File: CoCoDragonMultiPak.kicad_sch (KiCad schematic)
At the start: 51 parts, among them CN5 ATX-24, IC1 74LS245, IC10 74LS74, IC11 74LS153, IC12 74ALS30, IC13 GAL16V8, IC2 74LS367, IC3 74LS367, IC4 74LS367, IC5 74LS367, IC6 74LS367, IC7 74LS374, IC8 74LS368, IC9 74LS139, J1 CARTRIDGE EDGE, J2 CARTRIDGE EDGE, J3 CARTRIDGE EDGE, J4 CARTRIDGE EDGE, J5 CARTRIDGE EDGE, SW1 DEFAULT SLOT

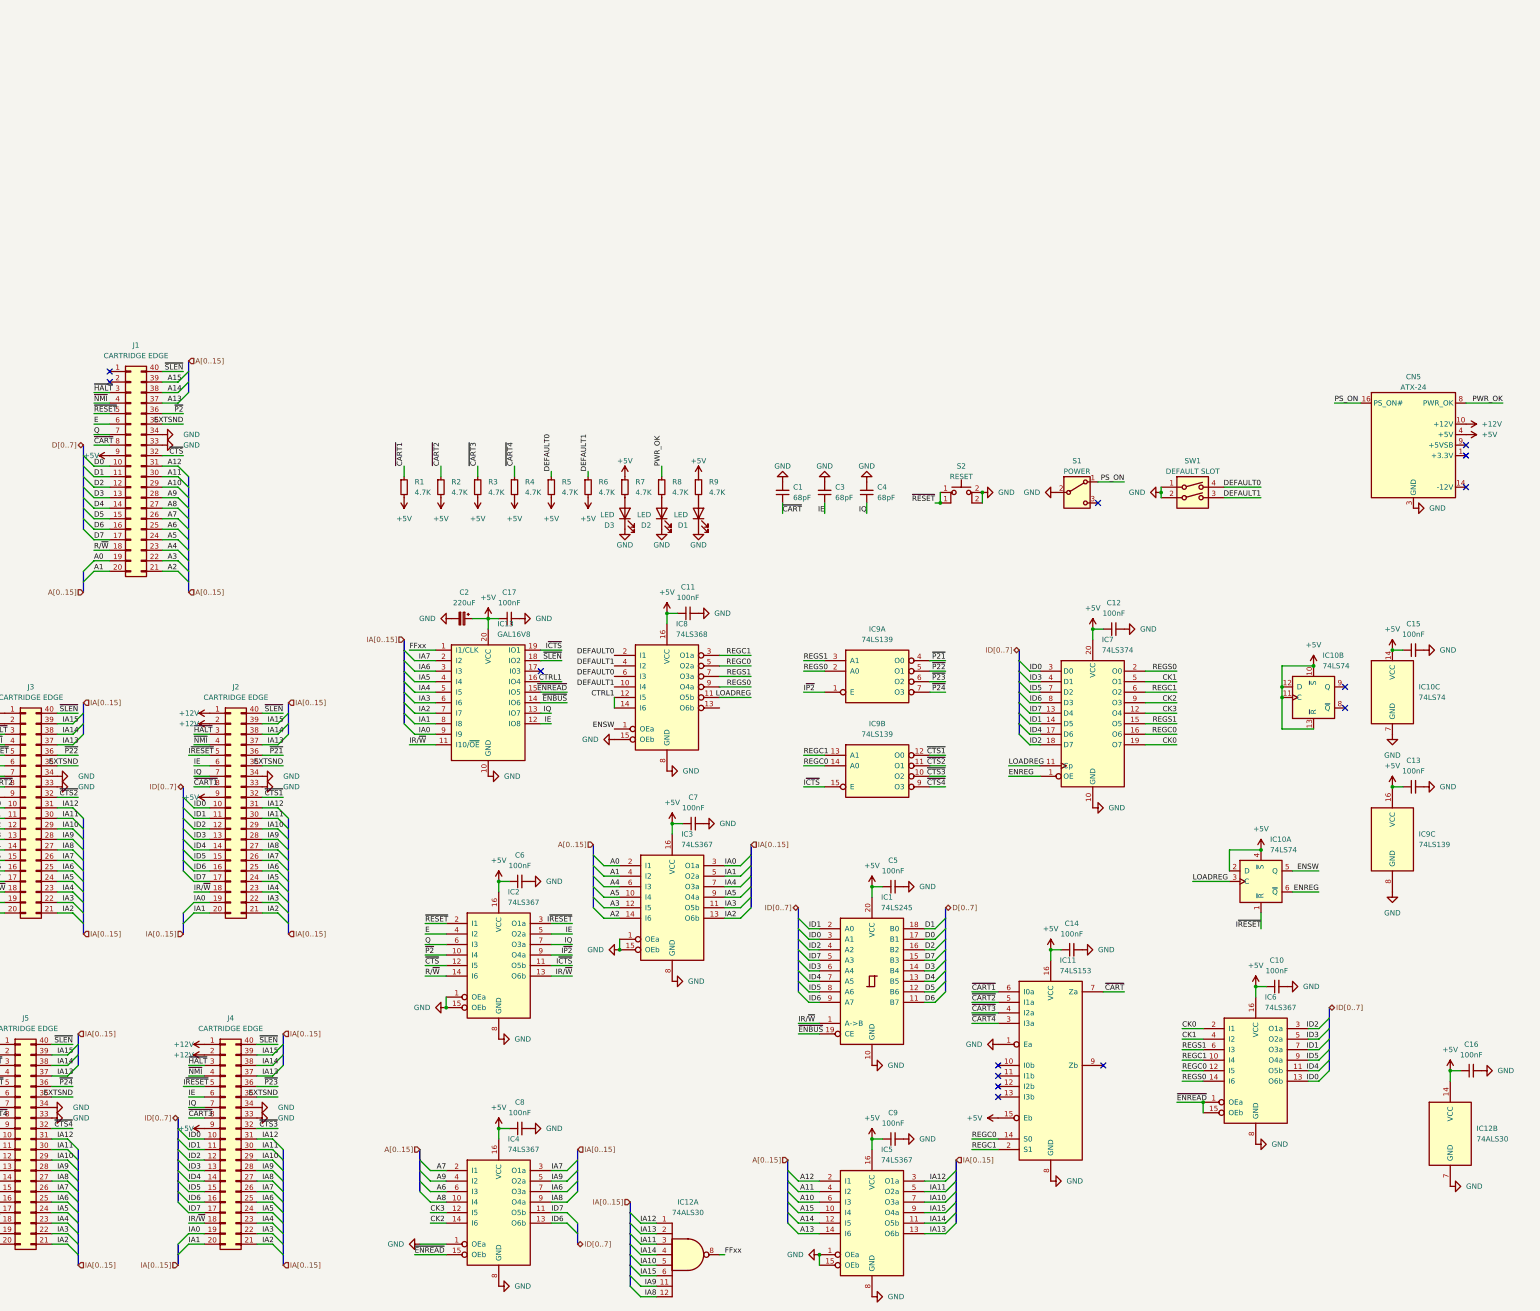
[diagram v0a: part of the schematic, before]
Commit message: convert to smd
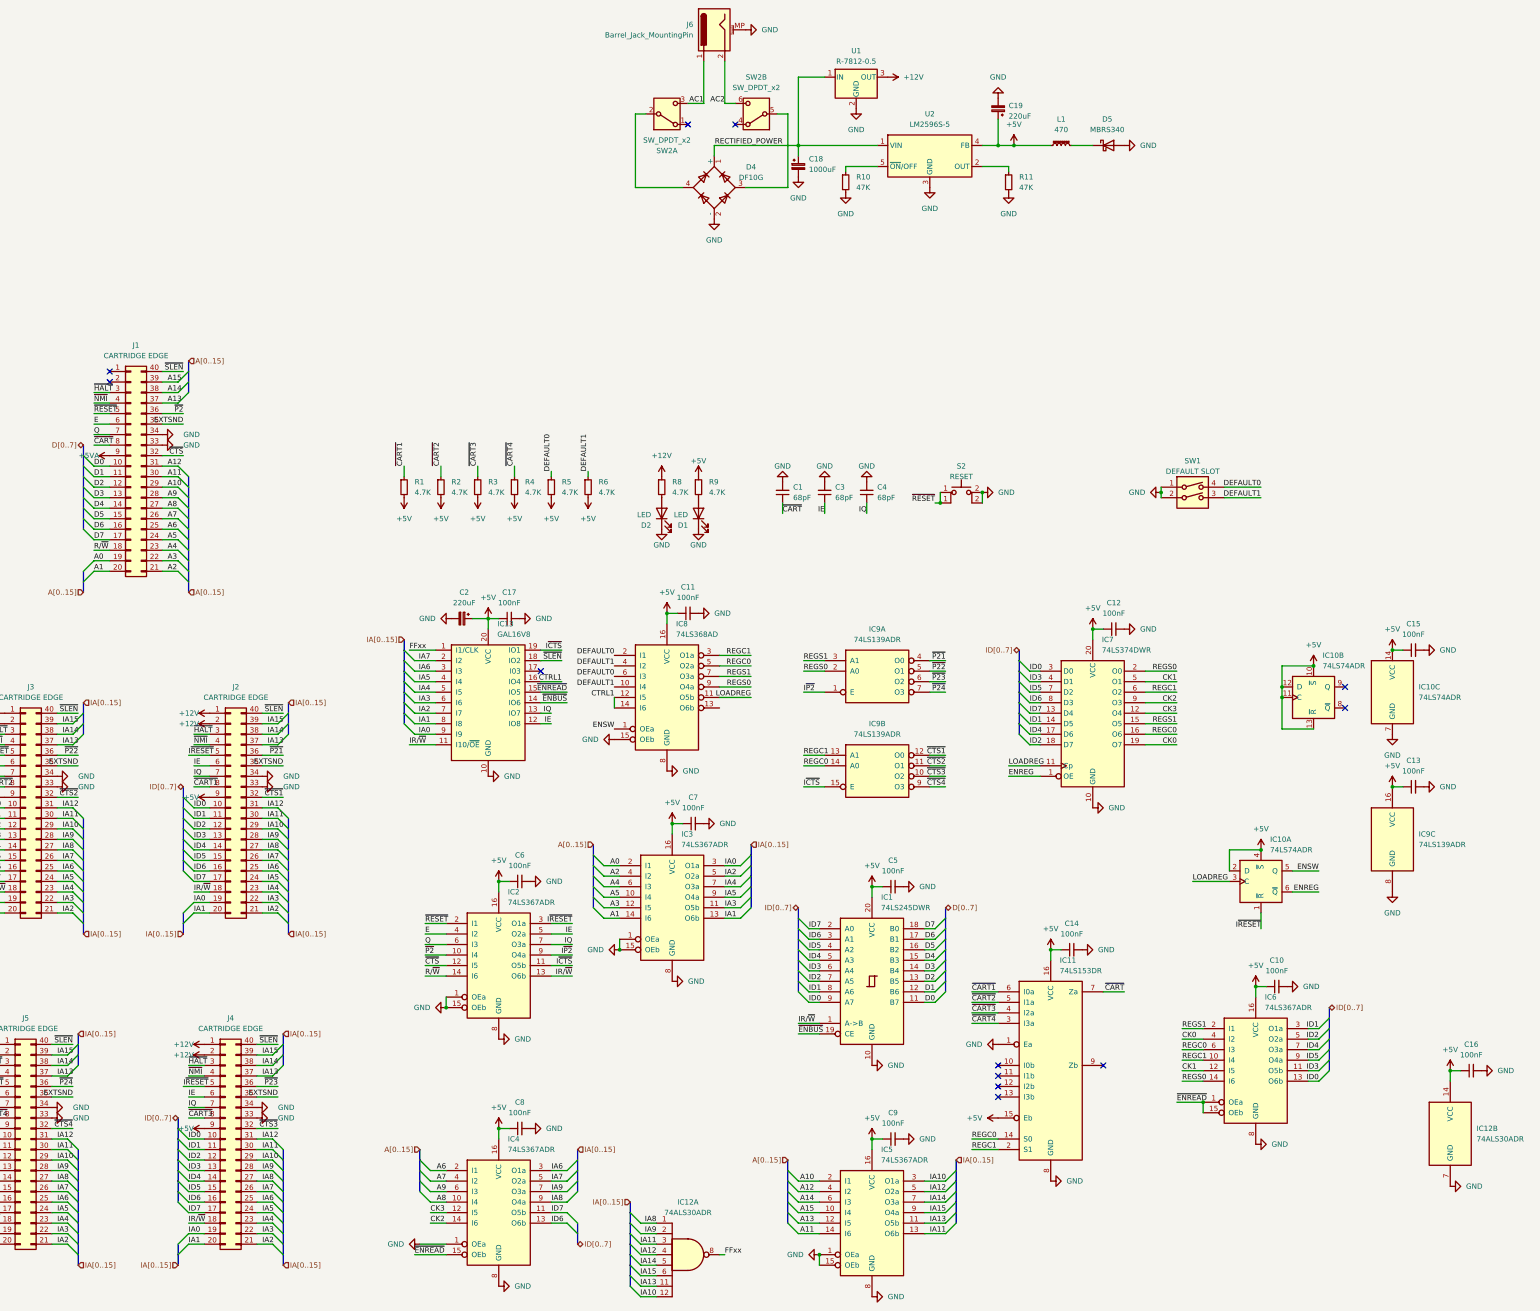
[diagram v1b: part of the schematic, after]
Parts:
- removed CN5: ATX-24, Connector_Molex:Molex_Mini-Fit_Jr_5566-24A_2x12_P4.20mm_Vertical, symbol Connector:ATX-24
- removed D3: LED, LED_THT:LED_D5.0mm, symbol Device:LED
- removed R7: 4.7K, Resistor_THT:R_Axial_DIN0207_L6.3mm_D2.5mm_P7.62mm_Horizontal, symbol Device:R_Small
- removed S1: POWER, Button_Switch_THT:SW_Slide-03_Wuerth-WS-SLTV_10x2.5x6.4_P2.54mm, symbol Switch:SW_SPDT
- added C18: 1000uF, Capacitor_SMD:CP_Elec_10x10.5, symbol Device:C_Polarized_Small
- added C19: 220uF, Capacitor_SMD:CP_Elec_6.3x5.4_Nichicon, symbol Device:C_Polarized_Small
- added D4: DF10G, Diode_THT:Diode_Bridge_DIP-4_W7.62mm_P5.08mm, symbol Diode_Bridge:DF10M
- added D5: MBRS340, Diode_SMD:D_SMC_Handsoldering, symbol Diode:1N5822
- added J6: Barrel_Jack_MountingPin, CoCoDragonMultiPak:Power_BarrelJack, symbol Connector:Barrel_Jack_MountingPin
- added L1: 470, Inductor_SMD:L_10.4x10.4_H4.8, symbol Device:L_Ferrite_Small
- added R10, R11: 47K, Resistor_SMD:R_0805_2012Metric_Pad1.20x1.40mm_HandSolder, symbol Device:R_Small
- added SW2: SW_DPDT_x2, CoCoDragonMultiPak:ALPS_DPDT_SPUN190900, symbol Switch:SW_DPDT_x2
- added U1: R-7812-0.5, Converter_DCDC:Converter_DCDC_RECOM_R-78E-0.5_THT, symbol Regulator_Switching:R-7812-0.5
- added U2: LM2596S-5, Package_TO_SOT_SMD:TO-263-5_TabPin3, symbol Regulator_Switching:LM2596S-5
- C1, C10, C11, C12, C13, C14, C15, C16, C17, C3, C4, C5, C6, C7, C8, C9: footprint Capacitor_THT:C_Disc_D3.4mm_W2.1mm_P2.50mm -> Capacitor_SMD:C_0805_2012Metric_Pad1.18x1.45mm_HandSolder
- C2: footprint Capacitor_THT:CP_Radial_D6.3mm_P2.50mm -> Capacitor_SMD:CP_Elec_6.3x5.4_Nichicon
- D1, D2: footprint LED_THT:LED_D5.0mm -> LED_SMD:LED_0805_2012Metric_Pad1.15x1.40mm_HandSolder
- IC1: value 74LS245 -> 74LS245DWR; footprint Package_DIP:DIP-20_W7.62mm_LongPads -> Package_SO:SOIC-20W_7.5x12.8mm_P1.27mm; DigiKey (none) -> 296-1214-1-ND
- IC10: value 74LS74 -> 74LS74ADR; footprint Package_DIP:DIP-14_W7.62mm_LongPads -> Package_SO:SOIC-14_3.9x8.7mm_P1.27mm; DigiKey (none) -> 296-14899-1-ND
- IC11: value 74LS153 -> 74LS153DR; footprint Package_DIP:DIP-16_W7.62mm_LongPads -> Package_SO:SOIC-16_3.9x9.9mm_P1.27mm; DigiKey (none) -> 296-SN74LS153DRCT-ND
- IC12: value 74ALS30 -> 74ALS30ADR; footprint Package_DIP:DIP-14_W7.62mm_LongPads -> Package_SO:SOIC-14_3.9x8.7mm_P1.27mm; DigiKey (none) -> SN74ALS30ADR-ND
- IC2, IC3, IC4, IC5, IC6: value 74LS367 -> 74LS367ADR; footprint Package_DIP:DIP-16_W7.62mm_LongPads -> Package_SO:SOIC-16_3.9x9.9mm_P1.27mm; DigiKey (none) -> 296-3700-1-ND
- IC7: value 74LS374 -> 74LS374DWR; footprint Package_DIP:DIP-20_W7.62mm_LongPads -> Package_SO:SOIC-20W_7.5x12.8mm_P1.27mm; DigiKey (none) -> 296-14894-1-ND
- IC8: value 74LS368 -> 74LS368AD; footprint Package_DIP:DIP-16_W7.62mm_LongPads -> Package_SO:SOIC-16_3.9x9.9mm_P1.27mm; DigiKey (none) -> 296-33998-5-ND
- IC9: value 74LS139 -> 74LS139ADR; footprint Package_DIP:DIP-16_W7.62mm_LongPads -> Package_SO:SOIC-16_3.9x9.9mm_P1.27mm; DigiKey (none) -> 296-31850-1-ND
- R1, R2, R3, R4, R5, R6, R8, R9: footprint Resistor_THT:R_Axial_DIN0207_L6.3mm_D2.5mm_P7.62mm_Horizontal -> Resistor_SMD:R_0805_2012Metric_Pad1.20x1.40mm_HandSolder
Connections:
- net PWR_OK is gone; now on net +12V: R8.1
- net +12V: now also U1.3 (OUT)
- net +5V: now also C19.1, L1.1, U2.4 (FB); no longer J1.9 (Pin_9)
- net A1: now also IC3.14 (I6); no longer IC3.4 (I2)
- net A10: now also IC5.2 (I1); no longer IC5.6 (I3)
- net A11: now also IC5.14 (I6); no longer IC5.4 (I2)
- net A12: now also IC5.4 (I2); no longer IC5.2 (I1)
- net A13: now also IC5.12 (I5); no longer IC5.14 (I6)
- net A14: now also IC5.6 (I3); no longer IC5.12 (I5)
- net A2: now also IC3.4 (I2); no longer IC3.14 (I6)
- net A6: now also IC4.2 (I1); no longer IC4.6 (I3)
- net A7: now also IC4.4 (I2); no longer IC4.2 (I1)
- net A9: now also IC4.6 (I3); no longer IC4.4 (I2)
- net CK0: now also IC6.4 (I2); no longer IC6.2 (I1)
- net CK1: now also IC6.12 (I5); no longer IC6.4 (I2)
- net D0: now also IC1.11 (B7); no longer IC1.17 (B1)
- net D1: now also IC1.12 (B6); no longer IC1.18 (B0)
- net D2: now also IC1.13 (B5); no longer IC1.16 (B2)
- net D4: now also IC1.15 (B3); no longer IC1.13 (B5)
- net D5: now also IC1.16 (B2); no longer IC1.12 (B6)
- net D6: now also IC1.17 (B1); no longer IC1.11 (B7)
- net D7: now also IC1.18 (B0); no longer IC1.15 (B3)
- net GND: now also C18.2, C19.2, D4.2 (-), D5.2 (A), J6.MP (MountPin), R10.2, R11.2, U1.2 (GND), U2.3 (GND)
- net IA1: now also IC3.13 (O6b); no longer IC3.5 (O2a)
- net IA10: now also IC12.12, IC5.3 (O1a); no longer IC12.5, IC5.7 (O3a)
- net IA11: now also IC5.13 (O6b); no longer IC5.5 (O2a)
- net IA12: now also IC12.4, IC5.5 (O2a); no longer IC12.1, IC5.3 (O1a)
- net IA13: now also IC12.11, IC5.11 (O5b); no longer IC12.2, IC5.13 (O6b)
- net IA14: now also IC12.5, IC5.7 (O3a); no longer IC12.4, IC5.11 (O5b)
- net IA2: now also IC3.5 (O2a); no longer IC3.13 (O6b)
- net IA6: now also IC4.3 (O1a); no longer IC4.7 (O3a)
- net IA7: now also IC4.5 (O2a); no longer IC4.3 (O1a)
- net IA8: now also IC12.1; no longer IC12.12
- net IA9: now also IC12.2, IC4.7 (O3a); no longer IC12.11, IC4.5 (O2a)
- net ID0: now also IC1.9 (A7); no longer IC1.3 (A1)
- net ID1: now also IC1.8 (A6), IC6.3 (O1a); no longer IC1.2 (A0), IC6.7 (O3a)
- net ID2: now also IC1.7 (A5), IC6.5 (O2a); no longer IC1.4 (A2), IC6.3 (O1a)
- net ID3: now also IC6.11 (O5b); no longer IC6.5 (O2a)
- net ID4: now also IC1.5 (A3), IC6.7 (O3a); no longer IC1.7 (A5), IC6.11 (O5b)
- net ID5: now also IC1.4 (A2); no longer IC1.8 (A6)
- net ID6: now also IC1.3 (A1); no longer IC1.9 (A7)
- net ID7: now also IC1.2 (A0); no longer IC1.5 (A3)
- net REGC0: now also IC6.6 (I3); no longer IC6.12 (I5)
- net REGS1: now also IC6.2 (I1); no longer IC6.6 (I3)
- new net: D4.3, SW2.5 (B)
- new net: R11.1, U2.2 (OUT)
- new net: R10.1, U2.5 (~{ON}/OFF)
- new net: D5.1 (K), L1.2
- new net: D4.4, SW2.2 (B)
- new net +5VA: J1.9 (Pin_9)
- new net AC1: J6.1, SW2.3 (C)
- new net AC2: J6.2, SW2.6 (C)
- new net RECTIFIED_POWER: C18.1, D4.1 (+), U1.1 (IN), U2.1 (VIN)
- no-connect marks 14 -> 12

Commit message: progress trace routing
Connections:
- net +5VA is gone; now on net +5V: J1.9 (Pin_9)
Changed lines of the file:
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@@
 		(on_board yes)
 		(dnp no)
-		(fields_autoplaced yes)
 		(property "Reference" "#PWR014"
 			(at 66.04 45.72 0)
@@
 			)
 		)
-		(property "Value" "+5VA"
-			(at 59.69 45.7199 90)
+		(property "Value" "+5V"
+			(at 58.166 44.45 90)
 			(effects
 				(font
 					(size 1.27 1.27)
 				)
-				(justify left)
 			)
 		)

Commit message: finish routing
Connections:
- net CTRL1: now also IC8.2 (I1); no longer IC8.14 (I6)
- net DEFAULT0: now also IC8.14 (I6), IC8.4 (I2); no longer IC8.2 (I1), IC8.6 (I3)
- net DEFAULT1: now also IC8.6 (I3); no longer IC8.4 (I2)
- net REGC0: now also IC8.7 (O3a); no longer IC8.5 (O2a)
- net REGC1: now also IC8.13 (O6b); no longer IC8.3 (O1a)
- net REGS1: now also IC8.5 (O2a); no longer IC8.7 (O3a)
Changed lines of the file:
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@@
 	(wire
 		(pts
-			(xy 184.15 104.14) (xy 184.15 106.68)
-		)
-		(stroke
-			(width 0)
-			(type default)
-		)
-	)
-	(wire
-		(pts
 			(xy 53.34 135.89) (xy 49.53 135.89)
 		)
@@
 	(wire
 		(pts
+			(xy 209.55 106.68) (xy 217.17 106.68)
+		)
+		(stroke
+			(width 0)
+			(type default)
+		)
+	)
+	(wire
+		(pts
 			(xy 172.72 105.41) (xy 166.37 105.41)
 		)
@@
 		)
 	)
-	(label "REGS1"
-		(at 217.17 99.06 180)
-		(fields_autoplaced yes)
-		(effects
-			(font
-				(size 1.27 1.27)
-			)
-			(justify right bottom)
-		)
-	)
 	(label "IA13"
 		(at 99.06 195.58 0)
@@
 		)
 	)
-	(label "ID2"
-		(at 81.28 215.9 0)
+	(label "REGC1"
+		(at 217.17 106.68 180)
 		(fields_autoplaced yes)
 		(effects
@@
 				(size 1.27 1.27)
 			)
-			(justify left bottom)
+			(justify right bottom)
 		)
 	)
-	(label "DEFAULT0"
-		(at 184.15 99.06 180)
+	(label "ID2"
+		(at 81.28 215.9 0)
 		(fields_autoplaced yes)
 		(effects
@@
 				(size 1.27 1.27)
 			)
-			(justify right bottom)
+			(justify left bottom)
 		)
 	)
@@
 		)
 	)
+	(label "REGS1"
+		(at 217.17 96.52 180)
+		(fields_autoplaced yes)
+		(effects
+			(font
+				(size 1.27 1.27)
+			)
+			(justify right bottom)
+		)
+	)
 	(label "IA12"
 		(at 194.31 238.76 180)
@@
 		)
 	)
-	(label "REGC1"
-		(at 217.17 93.98 180)
+	(label "DEFAULT1"
+		(at 184.15 99.06 180)
 		(fields_autoplaced yes)
 		(effects
@@
 		)
 	)
-	(label "REGC0"
-		(at 217.17 96.52 180)
-		(fields_autoplaced yes)
-		(effects
-			(font
-				(size 1.27 1.27)
-			)
-			(justify right bottom)
-		)
-	)
 	(label "~{CTS}"
 		(at 138.43 168.91 0)
@@
 		)
 	)
+	(label "DEFAULT0"
+		(at 184.15 106.68 180)
+		(fields_autoplaced yes)
+		(effects
+			(font
+				(size 1.27 1.27)
+			)
+			(justify right bottom)
+		)
+	)
 	(label "~{CART4}"
 		(at 31.75 205.74 0)
@@
 		)
 	)
+	(label "REGC0"
+		(at 217.17 99.06 180)
+		(fields_autoplaced yes)
+		(effects
+			(font
+				(size 1.27 1.27)
+			)
+			(justify right bottom)
+		)
+	)
 	(label "IE"
 		(at 234.95 59.69 180)
@@
 		)
 	)
-	(label "DEFAULT0"
-		(at 184.15 93.98 180)
-		(fields_autoplaced yes)
-		(effects
-			(font
-				(size 1.27 1.27)
-			)
-			(justify right bottom)
-		)
-	)
 	(label "IA14"
 		(at 100.33 113.03 0)
@@
 		)
 	)
-	(label "DEFAULT1"
-		(at 184.15 96.52 180)
-		(fields_autoplaced yes)
-		(effects
-			(font
-				(size 1.27 1.27)
-			)
-			(justify right bottom)
-		)
-	)
 	(label "A6"
 		(at 76.2 63.5 0)
@@
 		)
 	)
+	(label "CTRL1"
+		(at 184.15 93.98 180)
+		(fields_autoplaced yes)
+		(effects
+			(font
+				(size 1.27 1.27)
+			)
+			(justify right bottom)
+		)
+	)
 	(label "IA11"
 		(at 260.35 233.68 0)
@@
 		)
 	)
+	(label "DEFAULT0"
+		(at 184.15 96.52 180)
+		(fields_autoplaced yes)
+		(effects
+			(font
+				(size 1.27 1.27)
+			)
+			(justify right bottom)
+		)
+	)

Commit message: refine power circuit layout
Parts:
- J1: now left out of the parts list
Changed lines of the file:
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@@
 		(unit 1)
 		(exclude_from_sim no)
-		(in_bom yes)
+		(in_bom no)
 		(on_board yes)
 		(dnp no)

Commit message: revise layout
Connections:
- net +5V: no longer J1.9 (Pin_9)
- no-connect marks 12 -> 13
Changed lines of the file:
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@@
 	)
 	(no_connect
+		(at 62.23 45.72)
+	)
+	(no_connect
 		(at 213.36 -34.29)
 	)
@@
 					(unit 1)
 				)
-			)
-		)
-	)
-	(symbol
-		(lib_id "power:+5V")
-		(at 62.23 45.72 90)
-		(unit 1)
-		(exclude_from_sim no)
-		(in_bom yes)
-		(on_board yes)
-		(dnp no)
-		(property "Reference" "#PWR014"
-			(at 66.04 45.72 0)
-			(effects
-				(font
-					(size 1.27 1.27)
-				)
-				(hide yes)
-			)
-		)
-		(property "Value" "+5V"
-			(at 58.166 44.45 90)
-			(effects
-				(font
-					(size 1.27 1.27)
-				)
-			)
-		)
-		(property "Footprint" ""
-			(at 62.23 45.72 0)
-			(effects
-				(font
-					(size 1.27 1.27)
-				)
-				(hide yes)
-			)
-		)
-		(property "Datasheet" ""
-			(at 62.23 45.72 0)
-			(effects
-				(font
-					(size 1.27 1.27)
-				)
-				(hide yes)
-			)
-		)
-		(property "Description" "Power symbol creates a global label with name \"+5V\""
-			(at 62.23 45.72 0)
-			(effects
-				(font
-					(size 1.27 1.27)
-				)
-				(hide yes)
-			)
-		)
-		(pin "1"
-		)
-		(instances
-			(project "CoCoDragonMultiPak"
-				(path "/9d664c8a-4a7f-4204-988a-91326df86302"
-					(reference "#PWR014")
-					(unit 1)
-				)

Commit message: populate supplier specific part numbers
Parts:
- C1, C3, C4: DigiKey (none) -> 399-C0805C680J5GAC7800CT-ND; LCSC (none) -> C2363555
- C10, C11, C12, C13, C14, C15, C16, C17, C5, C6, C7, C8, C9: DigiKey (none) -> 399-C0805C104K5RAC7210CT-ND; LCSC (none) -> C2215757
- C18: DigiKey (none) -> 493-3930-1-ND; LCSC (none) -> C1668164
- C19, C2: DigiKey (none) -> 493-7373-1-ND; LCSC (none) -> C2162905
- D1, D2: DigiKey (none) -> 732-4984-1-ND; LCSC (none) -> C5353441
- D4: DigiKey (none) -> 641-1340-5-ND; LCSC (none) -> C5377
- D5: LCSC (none) -> C5563744
- IC1: LCSC (none) -> C129580
- IC10: LCSC (none) -> C39990
- IC11: LCSC (none) -> C1879872
- IC12: value 74ALS30ADR -> 74AHCT30D; DigiKey SN74ALS30ADR-ND -> 1727-74AHCT30D-Q100JCT-ND; LCSC (none) -> C7759
- IC13: DigiKey (none) -> ATF16V8C-7PU-ND; LCSC (none) -> C613484
- IC2, IC3, IC4, IC5, IC6: LCSC (none) -> C7655
- IC7: LCSC (none) -> C7763
- IC8: LCSC (none) -> C1548524
- IC9: LCSC (none) -> C7738
- J2, J3, J4, J5: DigiKey (none) -> 3-583717-1-ND; LCSC (none) -> C5173303
- L1: DigiKey (none) -> 495-2016-1-ND; LCSC (none) -> C7431106
- R1, R2, R3, R4, R5, R6, R8, R9: DigiKey (none) -> 541-4131-1-ND; LCSC (none) -> C269341
- R10, R11: DigiKey (none) -> 541-RCC080547K0FKEACT-ND; LCSC (none) -> C706300
- U1: DigiKey (none) -> 945-1032-ND; LCSC (none) -> C5199925
- U2: DigiKey (none) -> LM2596S-5.0/NOPB-ND; LCSC (none) -> C7419980

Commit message: update to rev 0.2
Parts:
- removed R11: 47K, Resistor_SMD:R_0805_2012Metric_Pad1.20x1.40mm_HandSolder, symbol Device:R_Small
- R10: value 47K -> 4K7
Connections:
- net +5V: now also L1.2; no longer L1.1
- net at U2.2 (OUT): now also D5.1 (K), L1.1
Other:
- note added: "X"
- moved on the sheet: C17, C2, D5, IC13, L1
